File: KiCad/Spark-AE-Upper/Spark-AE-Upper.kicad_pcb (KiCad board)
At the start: 2 copper layers, 50 x 100 mm, 21 parts, among them J1 SSM-120-L-SV-BE, J2 SSM-120-L-SV-BE, J3 Conn_02x10_Odd_Even, J4 Conn_02x05_Odd_Even, J5 Conn_01x08_Socket, J6 Conn_01x08_Socket, J7 UJ32-C-V-G-TH-5-P24-TR, SW1 SW_Push, SW2 SW_Push, U1 PJS008U-3000-0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

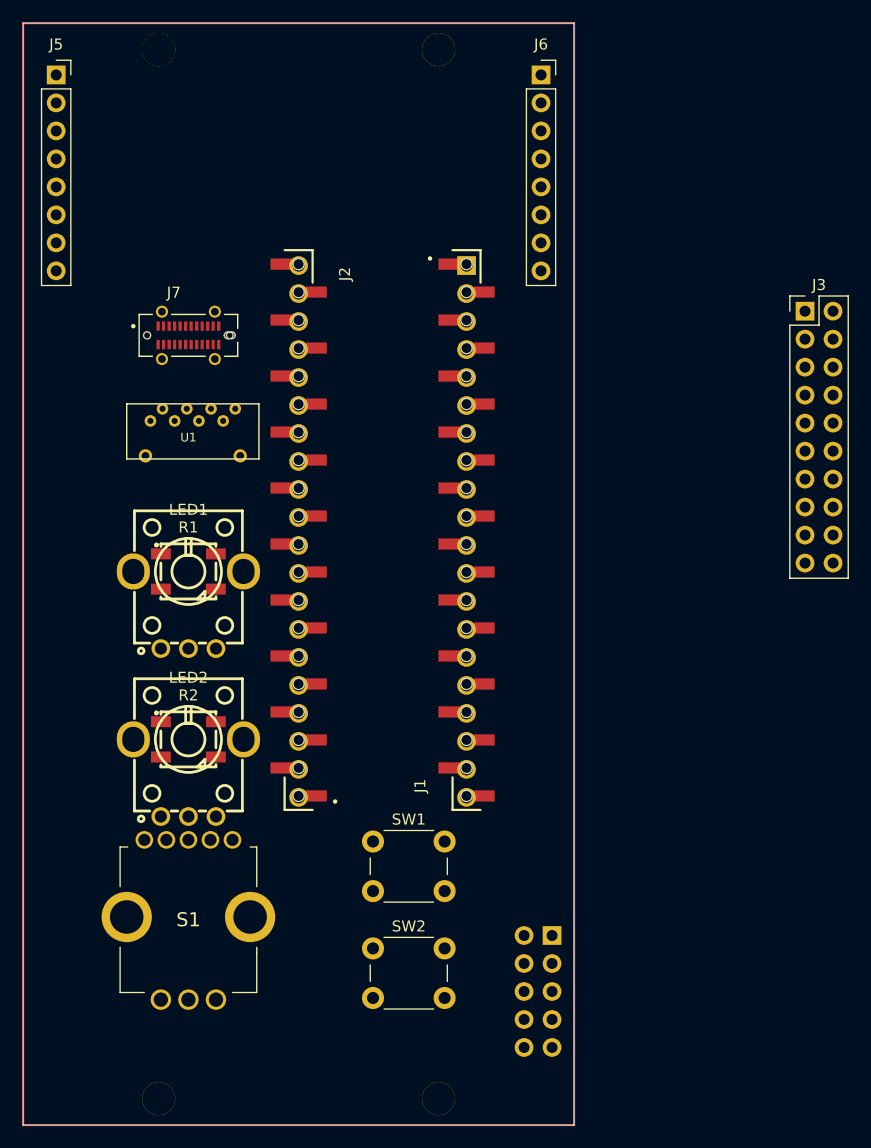
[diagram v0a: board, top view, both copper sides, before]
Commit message: positioned arc connector and repositioned daisy seed
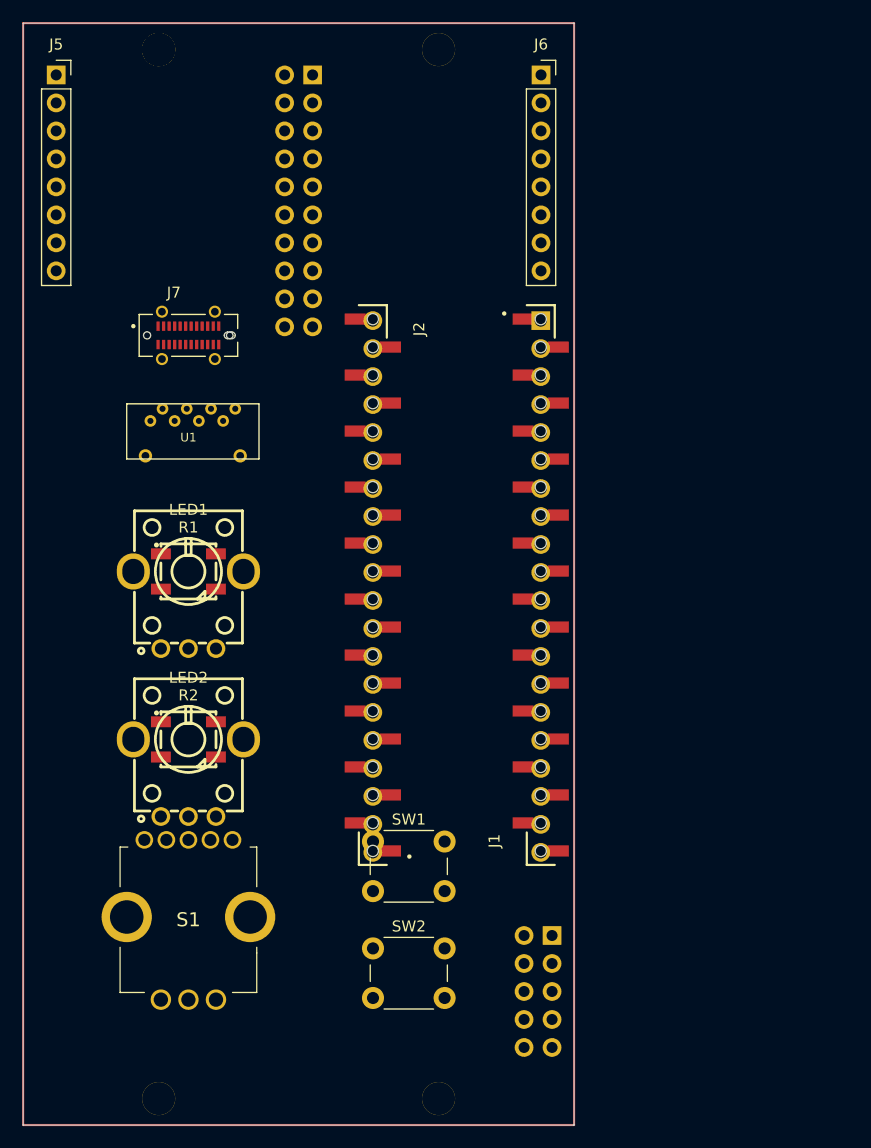
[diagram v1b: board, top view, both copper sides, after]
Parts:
- J3: moved to B.Cu
- moved J3 49.6 mm to (121.8, 53.7), turned to 180 degrees
- moved J1 8.39 mm to (142.5, 100.0)
- moved J2 8.39 mm to (127.3, 100.0)
- moved U2 8.39 mm to (142.5, 76.0)

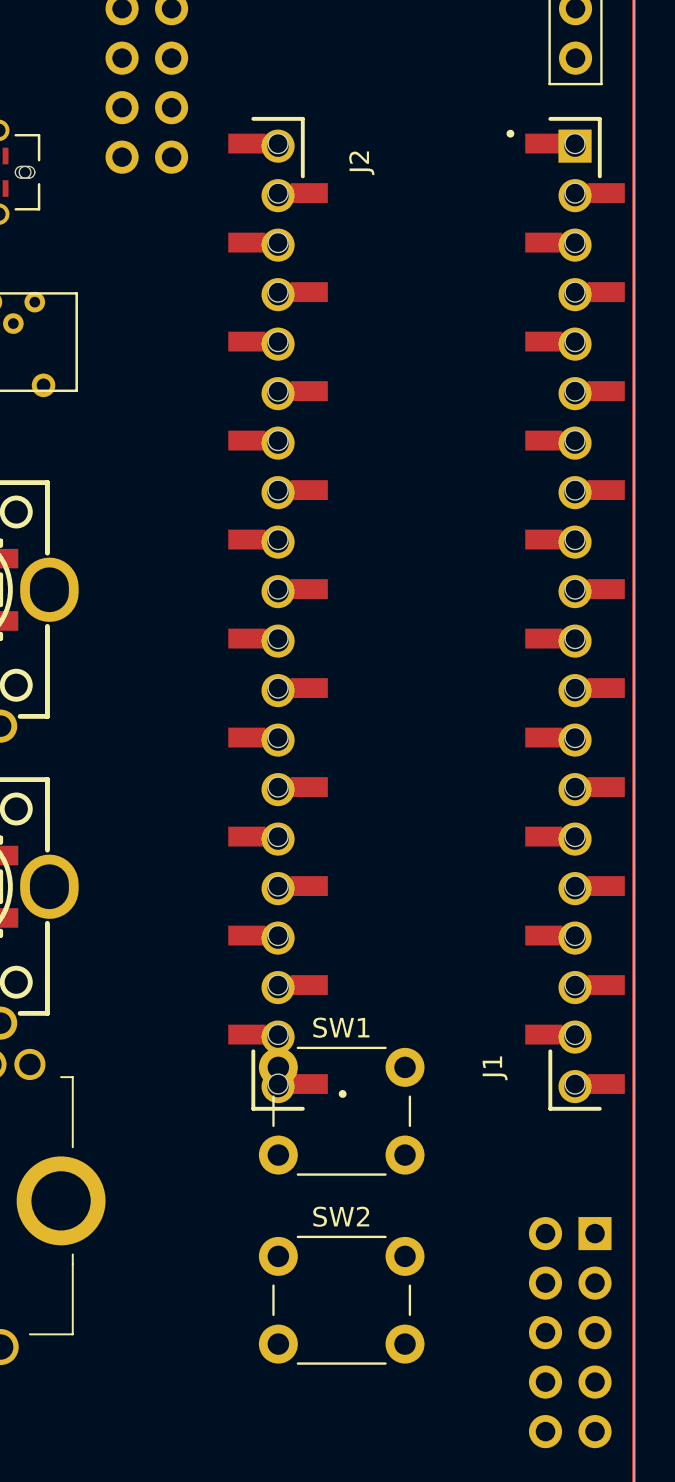
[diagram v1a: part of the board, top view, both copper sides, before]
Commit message: repositioned switches
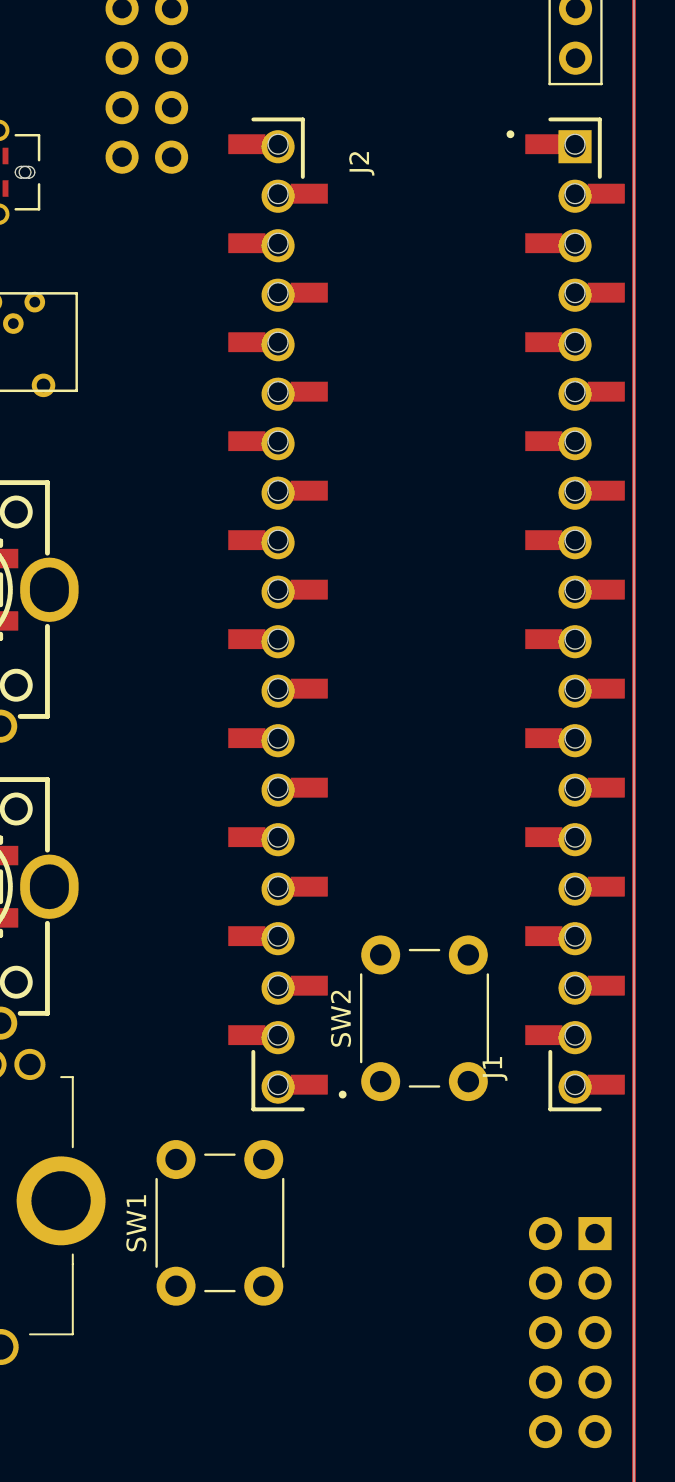
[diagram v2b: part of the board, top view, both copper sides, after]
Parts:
- moved SW1 12.4 mm to (122.1, 134.5), turned to 90 degrees
- moved SW2 10.4 mm to (132.6, 124.0), turned to 90 degrees
